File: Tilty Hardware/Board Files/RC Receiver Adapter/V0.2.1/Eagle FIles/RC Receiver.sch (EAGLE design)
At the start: 29 parts, among them U1 ATMEGA328P, U2 LM2931, U3 AP7313SOT23R, U4 C74HC407514-SOIC, Y1 16MHz

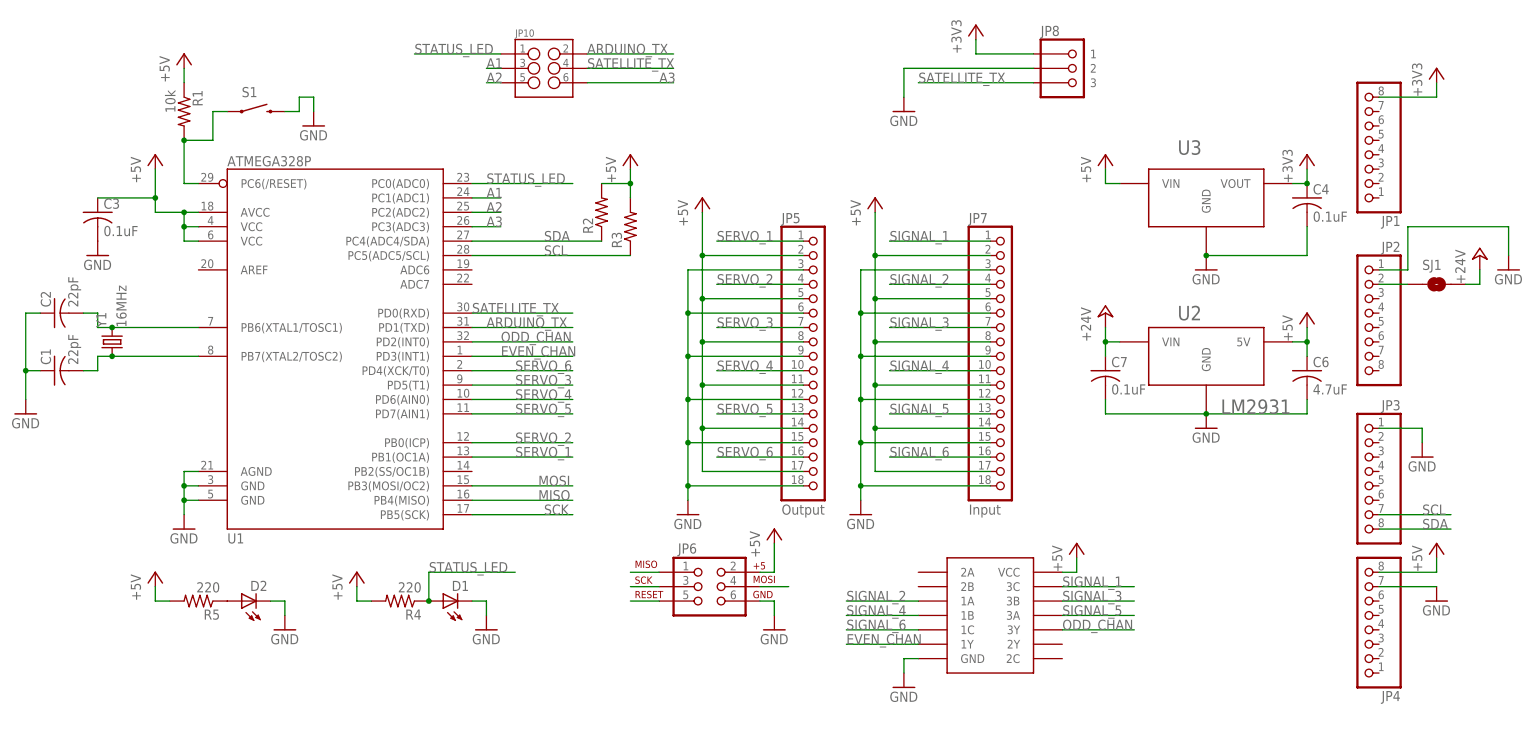
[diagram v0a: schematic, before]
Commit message: Semi-major revision to R/C Receiver adapter
All signals are now read by individual inputs and are no longer
interrupt driven. However the connection order will no longer matter,
and servo and R/C channels can be mixed.
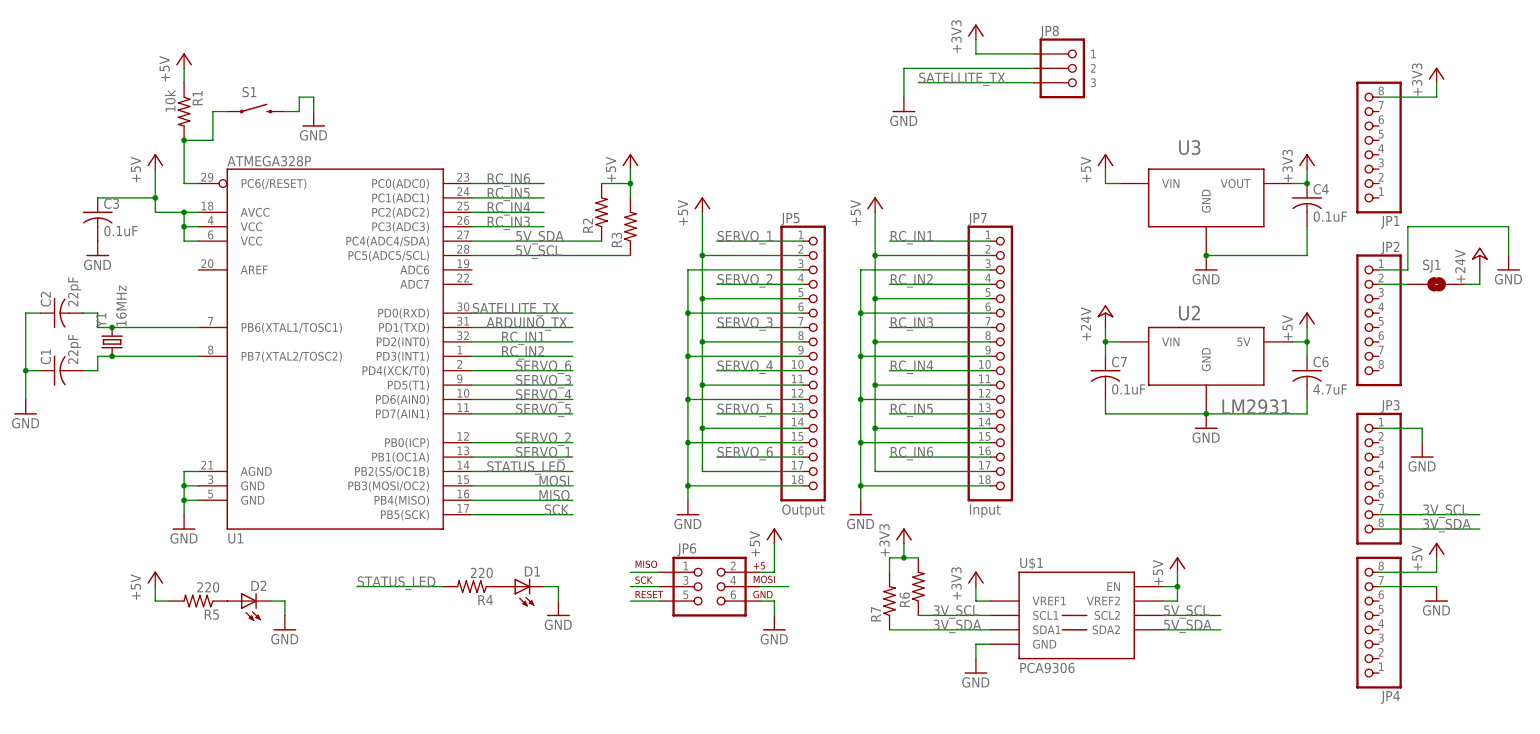
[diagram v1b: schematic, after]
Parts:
- removed JP10: (no value), SparkFun-Connectors:M03X2NO_SILK
- removed U4: C74HC407514-SOIC, My Parts:C74HC407514-SOIC
- added R6, R7: (no value), resistor:R-US_R0603
- added U$1: PCA9306, My Parts:PCA9306
- SJ1: value SOLDERJUMPERNC -> SOLDERJUMPERTRACE; device SparkFun-Passives:SOLDERJUMPERNC -> SparkFun-Passives:SOLDERJUMPERTRACE
- U3: PART# (none) -> AP7313-33SRG-7
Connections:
- removed net A1: JP10.3, U1.PC1(ADC1)
- removed net A2: JP10.5, U1.PC2(ADC2)
- removed net A3: JP10.6, U1.PC3(ADC3)
- removed net EVEN_CHAN: U1.PD3(INT1), U4.1Y
- removed net ODD_CHAN: U1.PD2(INT0), U4.3Y
- removed net SCL: JP3.7, R3.1, U1.PC5(ADC5/SCL)
- removed net SDA: JP3.8, R2.1, U1.PC4(ADC4/SDA)
- removed net SIGNAL_1: JP7.1, U4.3C
- removed net SIGNAL_2: JP7.4, U4.1A
- removed net SIGNAL_3: JP7.7, U4.3B
- removed net SIGNAL_4: JP7.10, U4.1B
- removed net SIGNAL_5: JP7.13, U4.3A
- removed net SIGNAL_6: JP7.16, U4.1C
- new net 3V_SCL: JP3.7, R6.1, U$1.SCL1
- new net 3V_SDA: JP3.8, R7.1, U$1.SDA1
- new net 5V_SCL: R3.1, U$1.SCL2, U1.PC5(ADC5/SCL)
- new net 5V_SDA: R2.1, U$1.SDA2, U1.PC4(ADC4/SDA)
- new net N$6: D1.A, R4.1
- new net RC_IN1: JP7.1, U1.PD2(INT0)
- new net RC_IN2: JP7.4, U1.PD3(INT1)
- new net RC_IN3: JP7.7, U1.PC3(ADC3)
- new net RC_IN4: JP7.10, U1.PC2(ADC2)
- new net RC_IN5: JP7.13, U1.PC1(ADC1)
- new net RC_IN6: JP7.16, U1.PC0(ADC0)
- net +3V3: now also R6.2, R7.2, U$1.VREF1
- net +5V: now also U$1.EN, U$1.VREF2; no longer R4.2, U4.VCC
- net ARDUINO_TX: no longer JP10.2
- net GND: now also U$1.GND; no longer U4.GND
- net SATELLITE_TX: no longer JP10.4
- net STATUS_LED: now also R4.2, U1.PB2(SS/OC1B); no longer D1.A, JP10.1, R4.1, U1.PC0(ADC0)
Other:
- moved on the sheet: D1, R4

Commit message: Updated R/C adapter silkscreen
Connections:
- net ARDUINO_TX renamed TX
- net SATELLITE_TX renamed RX
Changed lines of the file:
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@@
 <attribute name="PART#" x="190.5" y="121.92" size="1.778" layer="96" display="off"/>
 </instance>
-<instance part="+3V1" gate="G$1" x="175.26" y="129.54"/>
-<instance part="GND8" gate="1" x="162.56" y="114.3"/>
+<instance part="+3V1" gate="G$1" x="182.88" y="129.54"/>
+<instance part="GND8" gate="1" x="177.8" y="116.84"/>
 <instance part="U3" gate="G$1" x="215.9" y="101.6">
 <attribute name="PART#" x="215.9" y="101.6" size="1.778" layer="96" display="off"/>
@@
 <segment>
 <pinref part="JP8" gate="G$1" pin="2"/>
-<wire x1="185.42" y1="121.92" x2="162.56" y2="121.92" width="0.1524" layer="91"/>
-<wire x1="162.56" y1="121.92" x2="162.56" y2="116.84" width="0.1524" layer="91"/>
+<wire x1="185.42" y1="121.92" x2="177.8" y2="121.92" width="0.1524" layer="91"/>
+<wire x1="177.8" y1="121.92" x2="177.8" y2="119.38" width="0.1524" layer="91"/>
 <pinref part="GND8" gate="1" pin="GND"/>
 </segment>
@@
 </segment>
 </net>
-<net name="SATELLITE_TX" class="0">
+<net name="RX" class="0">
 <segment>
 <pinref part="JP8" gate="G$1" pin="3"/>
-<label x="165.1" y="119.38" size="1.778" layer="95"/>
-<wire x1="185.42" y1="119.38" x2="165.1" y2="119.38" width="0.1524" layer="91"/>
+<label x="180.34" y="119.38" size="1.778" layer="95"/>
+<wire x1="185.42" y1="119.38" x2="180.34" y2="119.38" width="0.1524" layer="91"/>
 </segment>
 <segment>
 <pinref part="U1" gate="G$1" pin="PD0(RXD)"/>
-<wire x1="86.36" y1="78.74" x2="104.14" y2="78.74" width="0.1524" layer="91"/>
-<label x="86.36" y="78.74" size="1.778" layer="95"/>
+<wire x1="86.36" y1="78.74" x2="91.44" y2="78.74" width="0.1524" layer="91"/>
+<label x="88.9" y="78.74" size="1.778" layer="95"/>
 </segment>
 </net>
@@
 <segment>
 <pinref part="JP8" gate="G$1" pin="1"/>
-<wire x1="185.42" y1="124.46" x2="175.26" y2="124.46" width="0.1524" layer="91"/>
+<wire x1="185.42" y1="124.46" x2="182.88" y2="124.46" width="0.1524" layer="91"/>
 <pinref part="+3V1" gate="G$1" pin="+3V3"/>
-<wire x1="175.26" y1="124.46" x2="175.26" y2="127" width="0.1524" layer="91"/>
+<wire x1="182.88" y1="124.46" x2="182.88" y2="127" width="0.1524" layer="91"/>
 </segment>
 <segment>
@@
 </segment>
 </net>
-<net name="ARDUINO_TX" class="0">
+<net name="TX" class="0">
 <segment>
 <pinref part="U1" gate="G$1" pin="PD1(TXD)"/>
-<wire x1="86.36" y1="76.2" x2="104.14" y2="76.2" width="0.1524" layer="91"/>
+<wire x1="86.36" y1="76.2" x2="91.44" y2="76.2" width="0.1524" layer="91"/>
 <label x="88.9" y="76.2" size="1.778" layer="95"/>
 </segment>

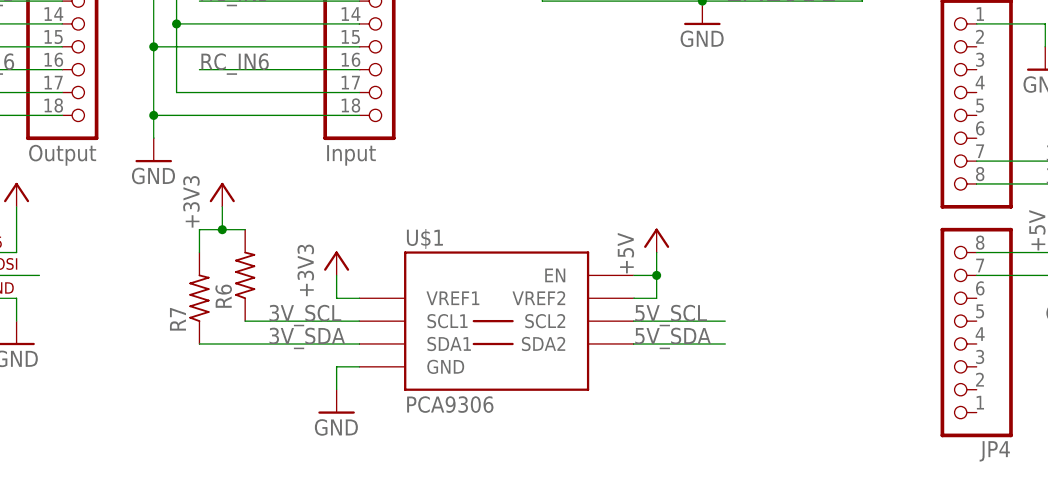
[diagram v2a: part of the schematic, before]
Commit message: Added solder jumper to disable I2C level translation
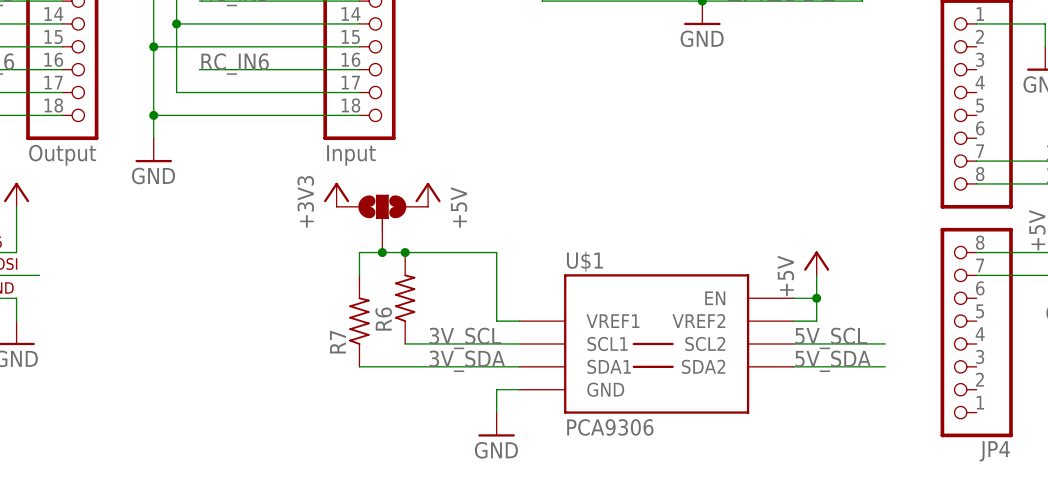
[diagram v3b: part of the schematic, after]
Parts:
- added SJ2: (no value), SparkFun-Passives:SOLDERJUMPER_2WAYS
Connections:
- new net N$7: R6.2, R7.2, SJ2.2, U$1.VREF1
- net +3V3: now also SJ2.1; no longer R6.2, R7.2, U$1.VREF1
- net +5V: now also SJ2.3
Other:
- moved on the sheet: R6, R7, U$1
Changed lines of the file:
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@@
 <part name="P+11" library="supply1" deviceset="+5V" device=""/>
 <part name="U$1" library="My Parts" deviceset="PCA9306" device=""/>
-<part name="+3V4" library="supply1" deviceset="+3V3" device=""/>
 <part name="P+6" library="supply1" deviceset="+5V" device=""/>
 <part name="GND7" library="supply1" deviceset="GND" device=""/>
@@
 <part name="R7" library="resistor" deviceset="R-US_" device="R0603"/>
 <part name="+3V5" library="supply1" deviceset="+3V3" device=""/>
+<part name="P+10" library="supply1" deviceset="+5V" device=""/>
+<part name="SJ2" library="SparkFun-Passives" deviceset="SOLDERJUMPER_2WAY" device="S"/>
 </parts>
 <sheets>
@@
 <instance part="GND16" gate="1" x="53.34" y="22.86"/>
 <instance part="P+11" gate="1" x="30.48" y="33.02"/>
-<instance part="U$1" gate="G$1" x="193.04" y="25.4"/>
-<instance part="+3V4" gate="G$1" x="175.26" y="33.02"/>
-<instance part="P+6" gate="1" x="210.82" y="35.56"/>
-<instance part="GND7" gate="1" x="175.26" y="15.24"/>
-<instance part="R6" gate="G$1" x="165.1" y="30.48" rot="R90"/>
-<instance part="R7" gate="G$1" x="160.02" y="27.94" rot="R90"/>
-<instance part="+3V5" gate="G$1" x="162.56" y="40.64"/>
+<instance part="U$1" gate="G$1" x="210.82" y="22.86"/>
+<instance part="P+6" gate="1" x="228.6" y="33.02"/>
+<instance part="GND7" gate="1" x="193.04" y="12.7"/>
+<instance part="R6" gate="G$1" x="182.88" y="27.94" rot="R90"/>
+<instance part="R7" gate="G$1" x="177.8" y="25.4" rot="R90"/>
+<instance part="+3V5" gate="G$1" x="175.26" y="40.64"/>
+<instance part="P+10" gate="1" x="185.42" y="40.64" rot="MR0"/>
+<instance part="SJ2" gate="G$1" x="180.34" y="38.1" smashed="yes" rot="R90">
+<attribute name="VALUE" x="182.245" y="40.64" size="1.778" layer="96" rot="R90"/>
+</instance>
 </instances>
 <busses>
@@
 <segment>
 <pinref part="U$1" gate="G$1" pin="GND"/>
-<wire x1="177.8" y1="20.32" x2="175.26" y2="20.32" width="0.1524" layer="91"/>
-<wire x1="175.26" y1="20.32" x2="175.26" y2="17.78" width="0.1524" layer="91"/>
+<wire x1="195.58" y1="17.78" x2="193.04" y2="17.78" width="0.1524" layer="91"/>
+<wire x1="193.04" y1="17.78" x2="193.04" y2="15.24" width="0.1524" layer="91"/>
 <pinref part="GND7" gate="1" pin="GND"/>
 </segment>
@@
 <pinref part="U$1" gate="G$1" pin="EN"/>
 <pinref part="P+6" gate="1" pin="+5V"/>
-<wire x1="208.28" y1="30.48" x2="210.82" y2="30.48" width="0.1524" layer="91"/>
-<wire x1="210.82" y1="30.48" x2="210.82" y2="33.02" width="0.1524" layer="91"/>
-<wire x1="210.82" y1="30.48" x2="210.82" y2="27.94" width="0.1524" layer="91"/>
-<junction x="210.82" y="30.48"/>
+<wire x1="226.06" y1="27.94" x2="228.6" y2="27.94" width="0.1524" layer="91"/>
+<wire x1="228.6" y1="27.94" x2="228.6" y2="30.48" width="0.1524" layer="91"/>
+<wire x1="228.6" y1="27.94" x2="228.6" y2="25.4" width="0.1524" layer="91"/>
+<junction x="228.6" y="27.94"/>
 <pinref part="U$1" gate="G$1" pin="VREF2"/>
-<wire x1="210.82" y1="27.94" x2="208.28" y2="27.94" width="0.1524" layer="91"/>
+<wire x1="228.6" y1="25.4" x2="226.06" y2="25.4" width="0.1524" layer="91"/>
+</segment>
+<segment>
+<pinref part="SJ2" gate="G$1" pin="3"/>
+<pinref part="P+10" gate="1" pin="+5V"/>
 </segment>
 </net>
@@
 </segment>
 <segment>
-<pinref part="U$1" gate="G$1" pin="VREF1"/>
-<wire x1="177.8" y1="27.94" x2="175.26" y2="27.94" width="0.1524" layer="91"/>
-<wire x1="175.26" y1="27.94" x2="175.26" y2="30.48" width="0.1524" layer="91"/>
-<pinref part="+3V4" gate="G$1" pin="+3V3"/>
-</segment>
-<segment>
-<pinref part="R7" gate="G$1" pin="2"/>
-<wire x1="160.02" y1="33.02" x2="160.02" y2="35.56" width="0.1524" layer="91"/>
-<pinref part="R6" gate="G$1" pin="2"/>
-<wire x1="160.02" y1="35.56" x2="162.56" y2="35.56" width="0.1524" layer="91"/>
+<pinref part="SJ2" gate="G$1" pin="1"/>
 <pinref part="+3V5" gate="G$1" pin="+3V3"/>
-<wire x1="162.56" y1="35.56" x2="165.1" y2="35.56" width="0.1524" layer="91"/>
-<wire x1="162.56" y1="35.56" x2="162.56" y2="38.1" width="0.1524" layer="91"/>
-<junction x="162.56" y="35.56"/>
 </segment>
 </net>
@@
 <segment>
 <pinref part="U$1" gate="G$1" pin="SDA2"/>
-<wire x1="208.28" y1="22.86" x2="218.44" y2="22.86" width="0.1524" layer="91"/>
-<label x="208.28" y="22.86" size="1.778" layer="95"/>
+<wire x1="226.06" y1="20.32" x2="236.22" y2="20.32" width="0.1524" layer="91"/>
+<label x="226.06" y="20.32" size="1.778" layer="95"/>
 </segment>
 </net>
@@
 <segment>
 <pinref part="U$1" gate="G$1" pin="SCL2"/>
-<wire x1="208.28" y1="25.4" x2="218.44" y2="25.4" width="0.1524" layer="91"/>
-<label x="208.28" y="25.4" size="1.778" layer="95"/>
+<wire x1="226.06" y1="22.86" x2="236.22" y2="22.86" width="0.1524" layer="91"/>
+<label x="226.06" y="22.86" size="1.778" layer="95"/>
 </segment>
 </net>
@@
 <segment>
 <pinref part="U$1" gate="G$1" pin="SDA1"/>
-<wire x1="177.8" y1="22.86" x2="160.02" y2="22.86" width="0.1524" layer="91"/>
-<label x="167.64" y="22.86" size="1.778" layer="95"/>
+<wire x1="195.58" y1="20.32" x2="177.8" y2="20.32" width="0.1524" layer="91"/>
+<label x="185.42" y="20.32" size="1.778" layer="95"/>
 <pinref part="R7" gate="G$1" pin="1"/>
 </segment>
@@
 <segment>
 <pinref part="U$1" gate="G$1" pin="SCL1"/>
-<wire x1="177.8" y1="25.4" x2="165.1" y2="25.4" width="0.1524" layer="91"/>
-<label x="167.64" y="25.4" size="1.778" layer="95"/>
+<wire x1="195.58" y1="22.86" x2="182.88" y2="22.86" width="0.1524" layer="91"/>
+<label x="185.42" y="22.86" size="1.778" layer="95"/>
 <pinref part="R6" gate="G$1" pin="1"/>
 </segment>
@@
 </segment>
 </net>
+<net name="N$7" class="0">
+<segment>
+<pinref part="R7" gate="G$1" pin="2"/>
+<wire x1="177.8" y1="30.48" x2="177.8" y2="33.02" width="0.1524" layer="91"/>
+<pinref part="R6" gate="G$1" pin="2"/>
+<wire x1="177.8" y1="33.02" x2="180.34" y2="33.02" width="0.1524" layer="91"/>
+<pinref part="SJ2" gate="G$1" pin="2"/>
+<wire x1="180.34" y1="33.02" x2="182.88" y2="33.02" width="0.1524" layer="91"/>
+<junction x="180.34" y="33.02"/>
+<pinref part="U$1" gate="G$1" pin="VREF1"/>
+<wire x1="195.58" y1="25.4" x2="193.04" y2="25.4" width="0.1524" layer="91"/>
+<wire x1="193.04" y1="25.4" x2="193.04" y2="33.02" width="0.1524" layer="91"/>
+<wire x1="193.04" y1="33.02" x2="182.88" y2="33.02" width="0.1524" layer="91"/>
+<junction x="182.88" y="33.02"/>
+</segment>
+</net>
